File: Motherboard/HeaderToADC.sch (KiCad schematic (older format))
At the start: 28 parts

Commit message: Moving along
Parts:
- added R705, R706, R707: 0, Resistors_SMD:R_0805_HandSoldering, symbol R
- C701, C702, C703, C704, C705, C706, C707, C710, C711, C712, C713, C714, C715: renamed from C?; footprint (none) -> Capacitors_SMD:C_0603_HandSoldering
- C708, C709: renamed from C?; footprint (none) -> Capacitors_SMD:C_0805_HandSoldering
- D701: renamed from D?; value LED -> GREEN_LED; footprint (none) -> LEDs:LED_0805; Digikey P/N (none) -> 475-1410-1-ND; MFR P/N (none) -> LG R971-KN-1
- P701: renamed from P?; footprint (none) -> moboFootprints:interconnect_modules_2.54x2.54_1.14mmDiameter
- R701, R703: renamed from R?; footprint (none) -> Resistors_SMD:R_0805_HandSoldering
- R702, R704: renamed from R?; footprint (none) -> Resistors_SMD:R_0603_HandSoldering
- U1001: renamed from U?; footprint (none) -> Housings_SSOP:TSSOP-38_4.4x9.7mm_Pitch0.5mm; Digikey P/N (none) -> 296-23504-5-ND; MFR P/N (none) -> ADS7953SBDBT
- U702, U903: renamed from U?; footprint (none) -> TO_SOT_Packages_SMD:SOT-23-5_HandSoldering
- U704: renamed from U?; footprint (none) -> Housings_SSOP:TSSOP-8_3x3mm_Pitch0.65mm
- gave numbers to parts that had none: 1
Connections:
- net GND: now also C704.2, C708.1, C709.1, C710.1, C711.1, C712.1, C713.1, U704.4 (GND)
- net SCLK: now also R705.2; no longer U1001.32 (SCLK)
- net SDI: now also R707.2; no longer U1001.33 (SDI)
- net SDO: now also R706.2; no longer U1001.34 (SDO)
- net MUX_DATA renamed AINP
- new net: R705.1, U1001.32 (SCLK)
- new net: R707.1, U1001.33 (SDI)
- new net: R706.1, U1001.34 (SDO)
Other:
- note added: "SAT caps are 0805 footprint\n"

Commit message: Final edits -- awaiting review before sending out
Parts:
- removed C702, C704, C705, C707, C712: 1uF, Capacitors_SMD:C_0603_HandSoldering, symbol C
- removed C706: 150pF, Capacitors_SMD:C_0603_HandSoldering, symbol C
- removed C708, C709: SAT, Capacitors_SMD:C_0805_HandSoldering, symbol C
- removed C710, C715: 2.2uF, Capacitors_SMD:C_0603_HandSoldering, symbol C
- removed C714: 10nF, Capacitors_SMD:C_0603_HandSoldering, symbol C
- removed D701: GREEN_LED, LEDs:LED_0805, symbol LED
- removed R703: SAT, Resistors_SMD:R_0805_HandSoldering, symbol R
- removed R704: 300, Resistors_SMD:R_0603_HandSoldering, symbol R
- removed unit 3 of U1001
- removed unit 1 of U1001
- removed unit 2 of U1001
- removed U702: OPA192, TO_SOT_Packages_SMD:SOT-23-5_HandSoldering, symbol OPA656
- removed U704: REF5025_TI, Housings_SSOP:TSSOP-8_3x3mm_Pitch0.65mm, symbol REF2025_TI
- removed U903: LP2985-N, TO_SOT_Packages_SMD:SOT-23-5_HandSoldering, symbol LP2985-N
- added C802, C804, C805, C812: 1uF, Capacitors_SMD:C_0603_HandSoldering, symbol C
- added C806: 150pF, Capacitors_SMD:C_0603_HandSoldering, symbol C
- added C808, C809: SAT, Capacitors_SMD:C_0805_HandSoldering, symbol C
- added C810: 2.2uF, Capacitors_SMD:C_0603_HandSoldering, symbol C
- added R806: SAT, Resistors_SMD:R_0805_HandSoldering, symbol R
- added U802: OPA192, TO_SOT_Packages_SMD:SOT-23-5_HandSoldering, symbol OPA656
- added U804: REF5025_TI, Housings_SSOP:TSSOP-8_3x3mm_Pitch0.65mm, symbol REF2025_TI
- added unit 3 of U901
- added unit 1 of U901
- added unit 2 of U901
- P801: renamed from P701; footprint moboFootprints:interconnect_modules_2.54x2.54_1.14mmDiameter -> hyperCustom:3M_50pos_latching; Digikey P/N (none) -> MHS50N; Mfr. P/N (none) -> N3433-6302RB
- U901: renamed from U1001; footprint (none) -> moboFootprints:TSSOP-38_4.4x9.7mm_Pitch0.5mm
- renumbered C701 to C801, C703 to C803, C711 to C811, C713 to C813, R705 to R801, R706 to R802, R707 to R803, R701 to R804, R702 to R805
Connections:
- net +5V: now also P801.10 (P10), P801.17 (P17), P801.18 (P18), P801.21 (P21), P801.22 (P22), P801.29 (P29), P801.30 (P30), P801.33 (P33), P801.34 (P34), P801.5 (P5), P801.6 (P6), P801.9 (P9), C802.1, C805.2, C808.2, C809.2, C810.2, U802.5 (+Vs), U804.2 (Vin), U901.29 (+VA), U901.5 (+VA); no longer P801.19 (P19), P801.20 (P20), P801.31 (P31), P801.32 (P32), P801.37 (P37), P801.38 (P38), P801.43 (P43), P801.44 (P44), P801.7 (P7), P801.8 (P8)
- net AINP: now also C806.2, U901.8 (AINP)
- net CH0: now also P801.36 (P36), U901.28 (CH0); no longer P801.3 (P3)
- net CH1: now also P801.38 (P38), U901.27 (CH1); no longer P801.9 (P9)
- net CH10: now also P801.45 (P45), U901.16 (CH10); no longer P801.34 (P34)
- net CH11: now also P801.43 (P43), U901.15 (CH11); no longer P801.28 (P28)
- net CH12: now also P801.41 (P41), U901.14 (CH12); no longer P801.22 (P22)
- net CH13: now also P801.39 (P39), U901.13 (CH13); no longer P801.16 (P16)
- net CH14: now also P801.37 (P37), U901.12 (CH14); no longer P801.10 (P10)
- net CH15: now also P801.35 (P35), U901.11 (CH15); no longer P801.4 (P4)
- net CH2: now also P801.40 (P40), U901.26 (CH2); no longer P801.15 (P15)
- net CH3: now also P801.42 (P42), U901.25 (CH3); no longer P801.21 (P21)
- net CH4: now also P801.44 (P44), U901.24 (CH4); no longer P801.27 (P27)
- net CH5: now also P801.46 (P46), U901.23 (CH5); no longer P801.33 (P33)
- net CH6: now also P801.48 (P48), U901.22 (CH6); no longer P801.39 (P39)
- net CH7: now also P801.50 (P50), U901.21 (CH7); no longer P801.45 (P45)
- net CH8: now also P801.49 (P49), U901.18 (CH8); no longer P801.46 (P46)
- net CH9: now also P801.47 (P47), U901.17 (CH9); no longer P801.40 (P40)
- net GND: now also P801.15 (P15), P801.16 (P16), P801.19 (P19), P801.20 (P20), P801.27 (P27), P801.28 (P28), P801.3 (P3), P801.31 (P31), P801.32 (P32), P801.4 (P4), P801.7 (P7), P801.8 (P8), C802.2, C804.2, C805.1, C806.1, C808.1, C809.1, C810.1, C812.1, U802.2 (-Vs), U804.4 (GND), U901.10 (AGND), U901.19 (AGND), U901.20 (AGND), U901.3 (REFM), U901.30 (AGND), U901.35 (BDGND), U901.6 (AGND), U901.9 (AINM); no longer P801.17 (P17), P801.18 (P18), P801.29 (P29), P801.30 (P30), P801.35 (P35), P801.36 (P36), P801.41 (P41), P801.42 (P42), P801.47 (P47), P801.48 (P48), P801.5 (P5), P801.6 (P6)
- net GPIO0: now also U901.37 (GPIO0)
- net GPIO1: now also U901.38 (GPIO1)
- net GPIO2: now also U901.1 (GPIO2)
- net GPIO3: now also U901.2 (GPIO3)
- net MUX_OUT: now also U802.3 (+), U901.7 (MXO)
- net Vref: now also R806.1, U804.6 (Vout), U901.4 (REFP)
- net at R805.2: now also U802.1 (Vout), U802.4 (-)
- net at C811.2: now also U804.5 (TRIM/NR)
- new net: C812.2, R806.2
- new net +3V3: C804.1, U901.36 (+VBD)

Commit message: computer is dying
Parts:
- added R807: 0, Resistors_SMD:R_0805_HandSoldering, symbol R
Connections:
- net at R805.2, U802.1 (Vout): now also R807.1; no longer U802.4 (-)
- new net: R807.2, U802.4 (-)
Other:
- note added: "TODO ADD NC FLAG\n"
- note added: "TODO: 0 ohm on feedback in case we want to jump+filter"
- note added: "TODO: 500k or lower corner**"
- note added: "TODO: confirm ESR"

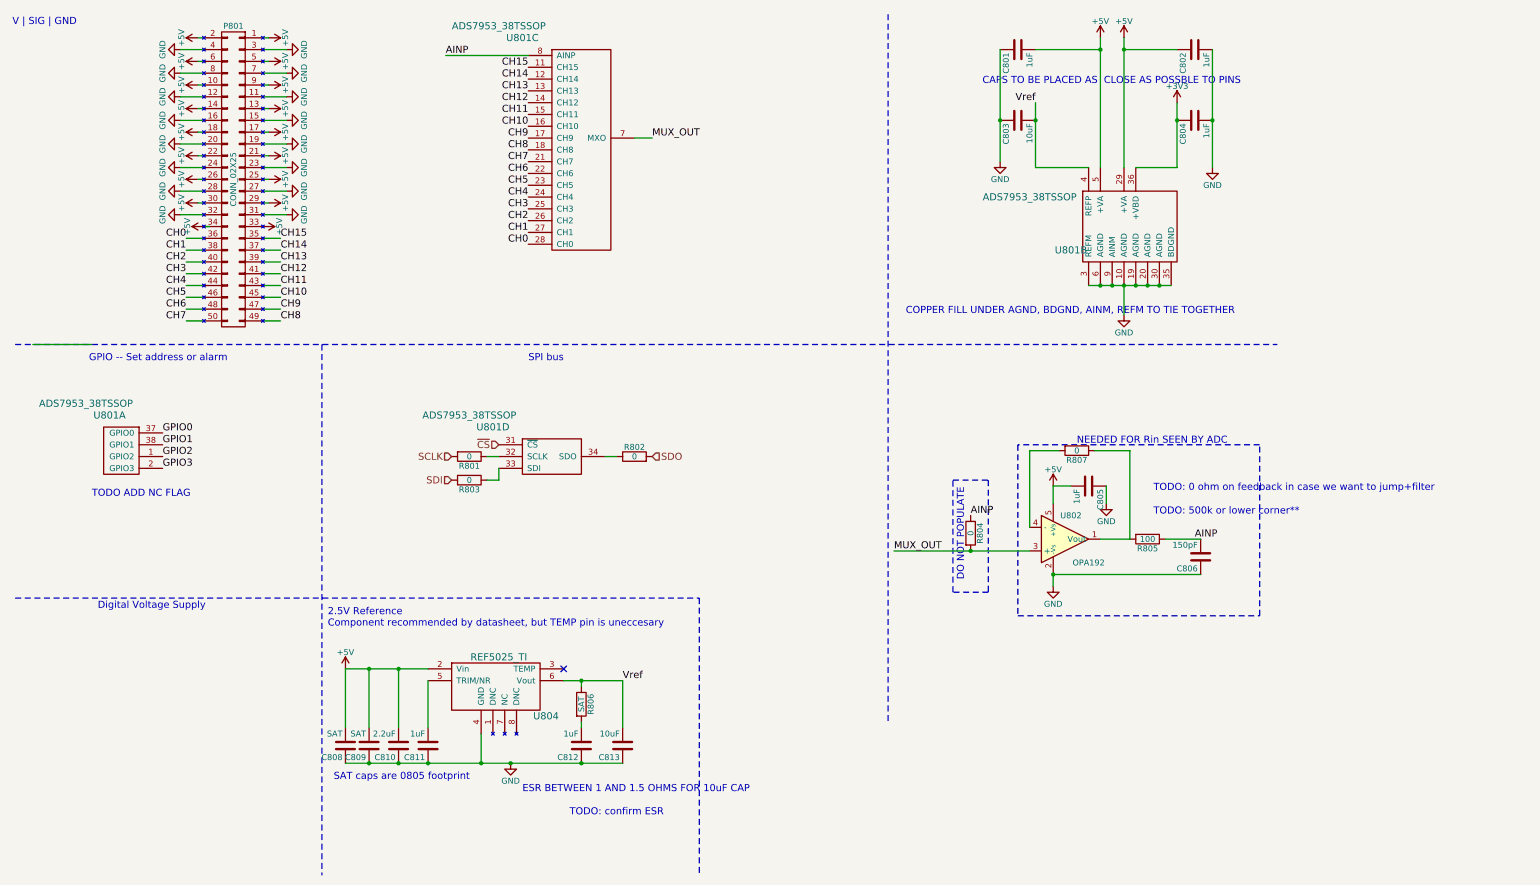
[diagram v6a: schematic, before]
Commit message: Mobo Version 2.1 Added Silk scren Ground Plane Cleanup Pinout changes on Beaglebone Headers, need to modify cabeling from V2.0 and earlier Added power sequencing for ADCs Removed Y3 ADC Removed TI Battery Board I2C lines More 5V connectors on Board Adjusted ADC Connecter pinout to match interface modules
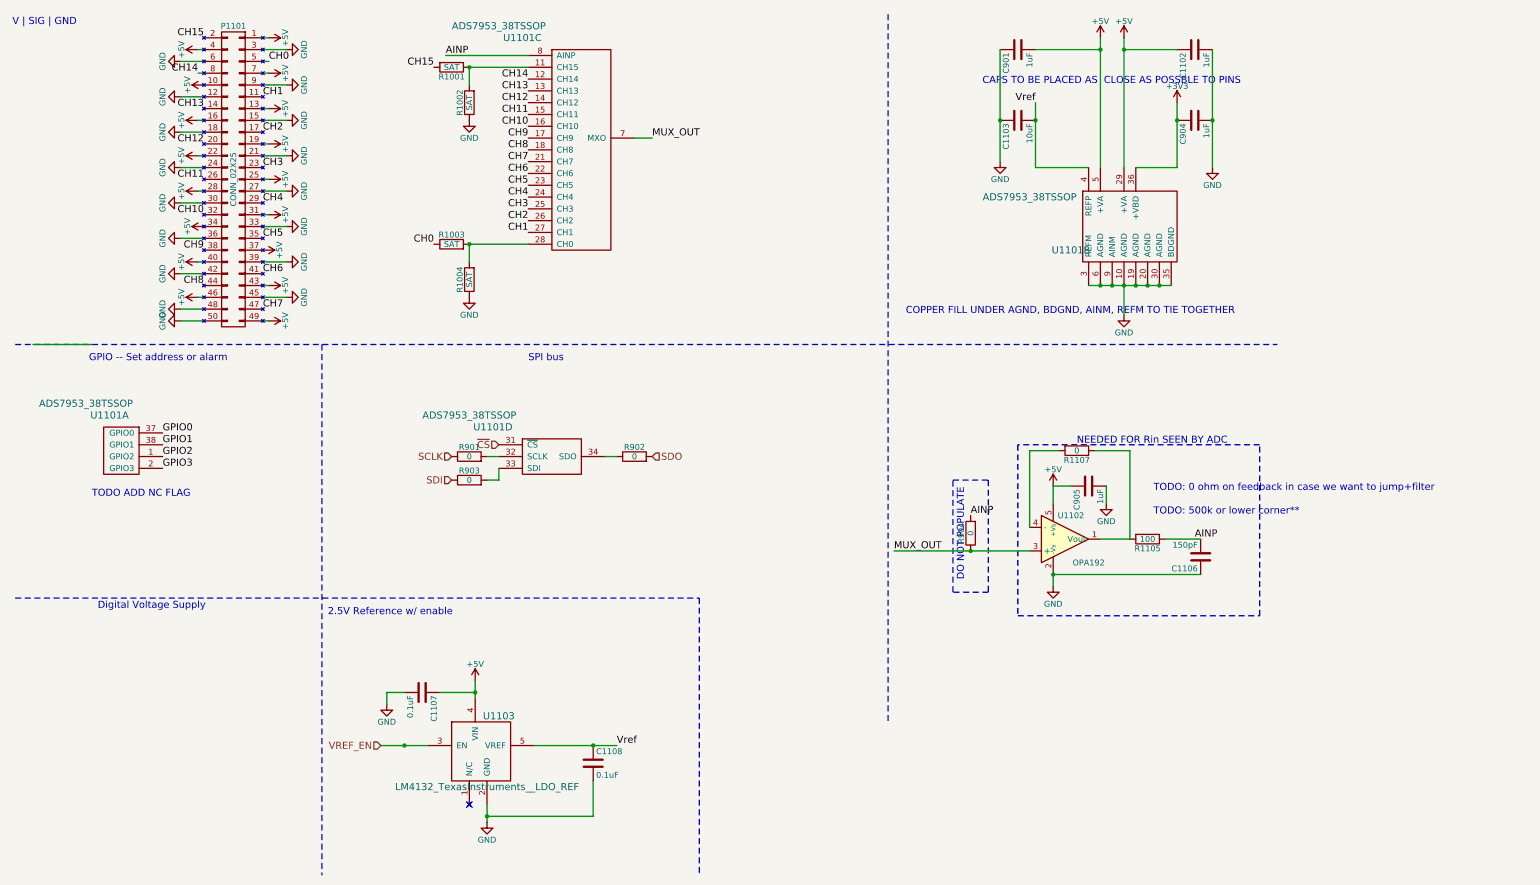
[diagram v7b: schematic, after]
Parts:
- removed C808, C809: SAT, Capacitors_SMD:C_0805_HandSoldering, symbol C
- removed C810: 2.2uF, Capacitors_SMD:C_0603_HandSoldering, symbol C
- removed C811, C812: 1uF, Capacitors_SMD:C_0603_HandSoldering, symbol C
- removed C813: 10uF, Capacitors_SMD:C_0603_HandSoldering, symbol C
- removed R801, R802, R803, R804: 0, Resistors_SMD:R_0805_HandSoldering, symbol R
- removed R806: SAT, Resistors_SMD:R_0805_HandSoldering, symbol R
- removed U804: REF5025_TI, Housings_SSOP:TSSOP-8_3x3mm_Pitch0.65mm, symbol REF2025_TI
- added C1108, C707: 0.1uF, Capacitors_SMD:C_0805_HandSoldering, symbol C
- added R1001, R1002, R1003, R710: SAT, Resistors_SMD:R_0805_HandSoldering, symbol R
- added R609, R701, R703, R704: 0, Resistors_SMD:R_0805_HandSoldering, symbol R
- added U803: LM4132_TexasInstruments__LDO_REF, TO_SOT_Packages_SMD:SOT-23-5_HandSoldering, symbol LM4132_TexasInstruments__LDO_REF
- C801, C802, C804, C805: Digikey P/N (none) -> 1276-1019-1-ND; Mfr P/N (none) -> CL10B105KO8NNNC
- C803: Digikey P/N (none) -> 1276-1948-1-ND; Mfr P/N (none) -> CL10B106MQ8NRNC
- C806: Digikey P/N (none) -> 732-7753-1-ND; Mfr P/N (none) -> 885012006009
- R805: Digikey P/N (none) -> 311-100HRCT-ND; Mfr P/N (none) -> RC0603FR-07100RL
- R807: Digikey P/N (none) -> 311-0.0ARTR-ND; Mfr P/N (none) -> RC0805JR-070RL
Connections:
- net +5V: now also C805.1, P801.16 (P16), P801.19 (P19), P801.28 (P28), P801.31 (P31), P801.37 (P37), P801.4 (P4), P801.40 (P40), P801.43 (P43), P801.46 (P46), P801.49 (P49), P801.7 (P7), C707.1, U803.4 (VIN); no longer C805.2, P801.14 (P14), P801.17 (P17), P801.18 (P18), P801.2 (P2), P801.21 (P21), P801.26 (P26), P801.29 (P29), P801.30 (P30), P801.33 (P33), P801.5 (P5), P801.6 (P6), P801.9 (P9)
- net AINP: now also R704.2
- net CH0: now also P801.5 (P5), R1003.1; no longer P801.36 (P36), U901.28 (CH0)
- net CH1: now also P801.11 (P11); no longer P801.38 (P38)
- net CH10: now also P801.32 (P32); no longer P801.45 (P45)
- net CH11: now also P801.26 (P26); no longer P801.43 (P43)
- net CH12: now also P801.20 (P20); no longer P801.41 (P41)
- net CH13: now also P801.14 (P14); no longer P801.39 (P39)
- net CH14: now also P801.8 (P8); no longer P801.37 (P37)
- net CH15: now also P801.2 (P2), R1001.2; no longer P801.35 (P35), U901.11 (CH15)
- net CH2: now also P801.17 (P17); no longer P801.40 (P40)
- net CH3: now also P801.23 (P23); no longer P801.42 (P42)
- net CH4: now also P801.29 (P29); no longer P801.44 (P44)
- net CH5: now also P801.35 (P35); no longer P801.46 (P46)
- net CH6: now also P801.41 (P41); no longer P801.48 (P48)
- net CH7: now also P801.47 (P47); no longer P801.50 (P50)
- net CH8: now also P801.44 (P44); no longer P801.49 (P49)
- net CH9: now also P801.38 (P38); no longer P801.47 (P47)
- net GND: now also C805.2, P801.18 (P18), P801.21 (P21), P801.30 (P30), P801.33 (P33), P801.36 (P36), P801.39 (P39), P801.42 (P42), P801.45 (P45), P801.48 (P48), P801.50 (P50), P801.6 (P6), P801.9 (P9), C1108.2, C707.2, R1002.1, R710.1, U803.2 (GND); no longer C805.1, P801.11 (P11), P801.16 (P16), P801.19 (P19), P801.20 (P20), P801.23 (P23), P801.28 (P28), P801.31 (P31), P801.32 (P32), P801.4 (P4), P801.7 (P7), P801.8 (P8)
- net MUX_OUT: now also R704.1
- net SCLK: now also R701.1
- net SDI: now also R703.1
- net SDO: now also R609.2
- net Vref: now also C1108.1, U803.5 (VREF)
- net at U901.32 (SCLK): now also R701.2
- net at U901.33 (SDI): now also R703.2
- net at U901.34 (SDO): now also R609.1
- new net: R1001.1, R1002.2, U901.11 (CH15)
- new net: R1003.2, R710.2, U901.28 (CH0)
- new net VREF_EN: U803.3 (EN)
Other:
- note added: "2.5V Reference w/ enable\n\n"
- note removed: "2.5V Reference\nComponent recommended by datasheet, but TEMP pin is uneccesary\n"
- note removed: "ESR BETWEEN 1 AND 1.5 OHMS FOR 10uF CAP\n\n"
- note removed: "SAT caps are 0805 footprint\n"
- note removed: "TODO: confirm ESR"
